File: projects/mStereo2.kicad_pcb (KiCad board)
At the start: 2 copper layers, 50.8 x 50.8 mm, 7 parts, among them J1 CONN_AMANERO, U1 ISO7240

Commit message: imported netlist to PcbNew, drew board outline and set origin
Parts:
- removed C1: 0.1, smd_transcriptic:SM0805_topbotrefs
- removed J1: CONN_AMANERO, sullins_gosselin:2x10_female
- removed MOUNT_M3.5 (x4): VAL**, mounting_transcriptic:MOUNT_M3.5
- removed U1: ISO7240, ti_gosselin:ISO7240
- added C101: 0.1, smd_gosselin:0805, F.Cu at (277.9, 56.5)
- added C102: 0.1, smd_gosselin:0805, F.Cu at (290.6, 36.2)
- added C103: 0.1, smd_gosselin:0805, F.Cu at (270.3, 61.7)
- added C104: 0.1, smd_gosselin:0805, F.Cu at (290.6, 38.8)
- added C105: 0.1, smd_gosselin:0805, F.Cu at (402.2, 45.8)
- added C106: 0.1, smd_gosselin:0805, F.Cu at (284.1, 108.4)
- added C107: 0.1, smd_gosselin:0805, F.Cu at (284.1, 105.8)
- added C201: 1, smd_gosselin:0805, F.Cu at (328.3, 105.7)
- added C202: 0.01, smd_gosselin:0805, F.Cu at (331.6, 103.1)
- added C203: 22, th_gosselin:CAP-POL-2.54-mm, F.Cu at (317.7, 105.5)
- added C301: 0.1, smd_gosselin:0805, F.Cu at (347.4, 38.8)
- added C302: 22, th_gosselin:CAP-POL-2.54-mm, F.Cu at (334.0, 53.6)
- added C303: 0.1, smd_gosselin:0805, F.Cu at (352.8, 41.4)
- added C304: 22, th_gosselin:CAP-POL-2.54-mm, F.Cu at (327.0, 53.6)
- added C305: 0.1, smd_gosselin:0805, F.Cu at (347.4, 43.9)
- added C306: 22, th_gosselin:CAP-POL-2.54-mm, F.Cu at (341.1, 41.2)
- added C307: 0.1, smd_gosselin:0805, F.Cu at (347.4, 41.4)
- added C308: 22, th_gosselin:CAP-POL-2.54-mm, F.Cu at (334.0, 41.2)
- added C309: 0.1, smd_gosselin:0805, F.Cu at (352.8, 38.8)
- added C310: 22, th_gosselin:CAP-POL-2.54-mm, F.Cu at (327.0, 41.2)
- added C311: 0.1, smd_gosselin:0805, F.Cu at (352.8, 36.2)
- added C312: 22, th_gosselin:CAP-POL-2.54-mm, F.Cu at (318.4, 54.7)
- added C401: 0.1, smd_gosselin:0805, F.Cu at (352.2, 71.2)
- added C402: 22, th_gosselin:CAP-POL-2.54-mm, F.Cu at (333.3, 88.5)
- added C403: 0.1, smd_gosselin:0805, F.Cu at (346.7, 78.9)
- added C404: 22, th_gosselin:CAP-POL-2.54-mm, F.Cu at (326.3, 88.5)
- added C405: 0.1, smd_gosselin:0805, F.Cu at (346.7, 73.8)
- added C406: 22, th_gosselin:CAP-POL-2.54-mm, F.Cu at (340.4, 76.2)
- added C407: 0.1, smd_gosselin:0805, F.Cu at (352.2, 76.3)
- added C408: 22, th_gosselin:CAP-POL-2.54-mm, F.Cu at (333.3, 76.2)
- added C409: 0.1, smd_gosselin:0805, F.Cu at (346.7, 76.3)
- added C410: 22, th_gosselin:CAP-POL-2.54-mm, F.Cu at (326.3, 76.2)
- added C411: 0.1, smd_gosselin:0805, F.Cu at (352.2, 73.8)
- added C412: 22, th_gosselin:CAP-POL-2.54-mm, F.Cu at (317.7, 89.7)
- added C501: 22, th_gosselin:CAP-POL-2.54-mm, F.Cu at (258.6, 110.8)
- added C502: 0.01, smd_gosselin:0805, F.Cu at (264.9, 114.9)
- added C503: 1, smd_gosselin:0805, F.Cu at (272.3, 110.6)
- added C601: 100, th_gosselin:CAP-POL-2.54-mm, F.Cu at (381.6, 96.5)
- added C602: 100, th_gosselin:CAP-POL-2.54-mm, F.Cu at (374.6, 96.5)
- added C603: 100, th_gosselin:CAP-POL-2.54-mm, F.Cu at (367.5, 96.5)
- added C604: 100, th_gosselin:CAP-POL-2.54-mm, F.Cu at (388.7, 96.5)
- added C605: 0.1, smd_gosselin:0805, F.Cu at (398.9, 109.3)
- added C606: 0.1, smd_gosselin:0805, F.Cu at (401.3, 91.5)
- added C607: 470p, th_gosselin:CAP-BOX-5.00-mm, F.Cu at (367.9, 107.6)
- added C608: 470p, th_gosselin:CAP-BOX-5.00-mm, F.Cu at (375.8, 107.6)
- added C701: 100, th_gosselin:CAP-POL-2.54-mm, F.Cu at (381.6, 70.5)
- added C702: 100, th_gosselin:CAP-POL-2.54-mm, F.Cu at (374.6, 70.5)
- added C703: 100, th_gosselin:CAP-POL-2.54-mm, F.Cu at (367.5, 70.5)
- added C704: 100, th_gosselin:CAP-POL-2.54-mm, F.Cu at (388.7, 70.5)
- added C705: 0.1, smd_gosselin:0805, F.Cu at (398.9, 83.3)
- added C706: 0.1, smd_gosselin:0805, F.Cu at (401.3, 65.6)
- added C707: 470p, th_gosselin:CAP-BOX-5.00-mm, F.Cu at (367.9, 81.6)
- added C708: 470p, th_gosselin:CAP-BOX-5.00-mm, F.Cu at (375.8, 81.6)
- added D101: AMBER_LED, smd_gosselin:1206_LED, F.Cu at (395.7, 41.2)
- added D102: GREEN_LED, smd_gosselin:1206_LED, F.Cu at (403.3, 37.3)
- added D103: RED_LED, smd_gosselin:1206_LED, F.Cu at (395.7, 36.9)
- added D104: GREEN_LED, smd_gosselin:1206_LED, F.Cu at (403.3, 42.1)
- added D105: GREEN_LED, smd_gosselin:1206_LED, F.Cu at (395.7, 46.0)
- added D201: GREEN_LED, smd_gosselin:1206_LED, F.Cu at (325.1, 101.7)
- added D301: RED_LED, smd_gosselin:1206_LED, F.Cu at (341.4, 49.2)
- added D401: RED_LED, smd_gosselin:1206_LED, F.Cu at (340.7, 84.2)
- added D501: GREEN_LED, smd_gosselin:1206_LED, F.Cu at (273.4, 106.9)
- added P101: CONN_AMANERO, sullins_gosselin:2x10_female, F.Cu at (261.3, 50.1)
- added P102: Screw-term 1x2, phoenix_gosselin:1x2, F.Cu at (288.8, 91.8)
- added P103: Screw-term 1X3, phoenix_gosselin:1x3, F.Cu at (290.3, 77.1)
- added P104: XLR-MALE, neutrik_gosselin:NC3MAAH-1, F.Cu at (269.2, 79.3)
- added P105: XLR-MALE, neutrik_gosselin:NC3MAAH-1, F.Cu at (378.9, 44.3)
- added R101: 121, smd_gosselin:0805, F.Cu at (372.9, 57.6)
- added R102: 121, smd_gosselin:0805, F.Cu at (389.3, 57.6)
- added R103: 121, smd_gosselin:0805, F.Cu at (367.5, 57.6)
- added R104: 825, smd_gosselin:0805, F.Cu at (383.8, 57.6)
- added R105: 825, smd_gosselin:0805, F.Cu at (378.4, 57.6)
- added R201: 121, smd_gosselin:0805, F.Cu at (331.6, 100.6)
- added R301: 121, smd_gosselin:0805, F.Cu at (347.4, 36.2)
- added R401: 121, smd_gosselin:0805, F.Cu at (346.7, 71.2)
- added R501: 121, smd_gosselin:0805, F.Cu at (272.3, 113.1)
- added R601: 1.21k, smd_gosselin:0805, F.Cu at (388.8, 103.9)
- added R602: 1.21k, smd_gosselin:0805, F.Cu at (394.3, 103.9)
- added R603: 1.21k, smd_gosselin:0805, F.Cu at (401.3, 94.1)
- added R604: 1.21k, smd_gosselin:0805, F.Cu at (394.3, 106.6)
- added R605: 2.49k, smd_gosselin:0805, F.Cu at (395.0, 98.4)
- added R606: 2.49k, smd_gosselin:0805, F.Cu at (400.5, 99.4)
- added R607: 1.21k, smd_gosselin:0805, F.Cu at (388.0, 110.8)
- added R608: 1.21k, smd_gosselin:0805, F.Cu at (393.4, 109.3)
- added R609: 1.21k, smd_gosselin:0805, F.Cu at (382.5, 110.8)
- added R610: 1.21k, smd_gosselin:0805, F.Cu at (400.5, 102.1)
- added R611: 2.49k, smd_gosselin:0805, F.Cu at (395.0, 101.1)
- added R612: 2.49k, smd_gosselin:0805, F.Cu at (399.7, 104.8)
- added R613: 10, smd_gosselin:0805, F.Cu at (388.8, 106.6)
- added R614: 10, smd_gosselin:0805, F.Cu at (401.3, 96.8)
- added R701: 1.21k, smd_gosselin:0805, F.Cu at (388.8, 78.0)
- added R702: 1.21k, smd_gosselin:0805, F.Cu at (394.3, 78.0)
- added R703: 1.21k, smd_gosselin:0805, F.Cu at (401.3, 68.2)
- added R704: 1.21k, smd_gosselin:0805, F.Cu at (394.3, 80.7)
- added R705: 2.49k, smd_gosselin:0805, F.Cu at (395.0, 72.5)
- added R706: 2.49k, smd_gosselin:0805, F.Cu at (400.5, 73.5)
- added R707: 1.21k, smd_gosselin:0805, F.Cu at (388.0, 84.9)
- added R708: 1.21k, smd_gosselin:0805, F.Cu at (393.4, 83.4)
- added R709: 1.21k, smd_gosselin:0805, F.Cu at (382.5, 84.9)
- added R710: 1.21k, smd_gosselin:0805, F.Cu at (400.5, 76.2)
- added R711: 2.49k, smd_gosselin:0805, F.Cu at (395.0, 75.2)
- added R712: 2.49k, smd_gosselin:0805, F.Cu at (399.7, 78.9)
- added R713: 10, smd_gosselin:0805, F.Cu at (388.8, 80.6)
- added R714: 10, smd_gosselin:0805, F.Cu at (401.3, 70.8)
- added U101: ISO7640, ti_gosselin:SOIC-16-W, F.Cu at (273.4, 43.1)
- added U102: CDCLVC1104, ti_gosselin:TSSOP-8, F.Cu at (283.2, 51.9)
- added U103: MCP100-315DI, microchip_gosselin:SOT-23-3, F.Cu at (395.1, 52.1)
- added U104: SRC4192, ti_gosselin:TSSOP-28, F.Cu at (283.5, 41.6)
- added U201: LT1761, linear_gosselin:SOT-23-5, F.Cu at (323.4, 107.5)
- added U301: WM8741, ti_gosselin:TSSOP-28, F.Cu at (319.1, 41.6)
- added U401: WM8741, ti_gosselin:TSSOP-28, F.Cu at (318.5, 76.6)
- added U501: LT1763, linear_gosselin:SOIC-8, F.Cu at (265.8, 109.1)
- added U601: OPA1632, ti_gosselin:MSOP-8-PWP, F.Cu at (382.9, 106.1)
- added U602: OPA1632, ti_gosselin:MSOP-8-PWP, F.Cu at (395.4, 93.7)
- added U701: OPA1632, ti_gosselin:MSOP-8-PWP, F.Cu at (382.9, 80.1)
- added U702: OPA1632, ti_gosselin:MSOP-8-PWP, F.Cu at (395.4, 67.8)
- added X101: XTAL, crystek_gosselin:XTAL-5x7mm, F.Cu at (271.3, 55.4)
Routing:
- net /VCC1: track 20.4 -> 0.00 mm
- net /GND1: track 19.6 -> 0.00 mm
- net Net-(J1-Pad2): track 15.9 -> 0.00 mm
- net Net-(J1-Pad3): track 15.3 -> 0.00 mm
- net Net-(J1-Pad4): track 14.7 -> 0.00 mm
- removed copper zone on B.Cu, net (none)
- removed copper zone on F.Cu, net (none)
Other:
- board size 50.8 x 50.8 mm -> 220 x 160 mm
- net class Default: clearance 0.127 -> 0.254; trace_width 0.1524 -> 0.254; via_dia 0.635 -> 0.889; via_drill 0.381 -> 0.635
- net class Power removed
- rule trace_clearance: 0.127 -> 0.254
- rule trace_min: 0.127 -> 0.254
- rule via_min_drill: 0.254 -> 0.508
- rule via_min_size: 0.254 -> 0.889
- board text removed: "board origin"

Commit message: prelimiary component positioning, board resizing, added mounting holes footprint
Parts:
- added mounting_m3: VAL**, mounting_gosselin:mounting_m3, F.Cu at (38.8, 38.8)
- added mounting_m3: VAL**, mounting_gosselin:mounting_m3, F.Cu at (190.7, 38.8)
- added mounting_m3: VAL**, mounting_gosselin:mounting_m3, F.Cu at (38.8, 151.2)
- added mounting_m3: VAL**, mounting_gosselin:mounting_m3, F.Cu at (190.7, 151.2)
- added mounting_m3: VAL**, mounting_gosselin:mounting_m3, F.Cu at (100.0, 116.8)
- added mounting_m3: VAL**, mounting_gosselin:mounting_m3, F.Cu at (100.0, 141.8)
- added mounting_m3: VAL**, mounting_gosselin:mounting_m3, F.Cu at (40.0, 141.8)
- added mounting_m3: VAL**, mounting_gosselin:mounting_m3, F.Cu at (40.0, 116.8)
- P101: moved to B.Cu
- moved D104 363.2 mm to (41.4, 72.8), turned to 180 degrees
- moved D102 363.1 mm to (41.4, 66.8)
- moved D103 355.1 mm to (41.4, 60.9)
- moved D105 354.8 mm to (41.4, 63.9)
- moved D101 354.5 mm to (41.4, 51.9)
- moved C105 341.7 mm to (65.5, 103.6)
- moved R102 341.5 mm to (47.9, 66.8)
- moved U103 338.8 mm to (60.4, 104.8)
- moved R104 336.3 mm to (47.9, 72.8), turned to 180 degrees
- moved R105 330.5 mm to (47.9, 63.9)
- moved R101 325.1 mm to (47.9, 51.9)
- moved R103 319.6 mm to (47.9, 60.9)
- moved D401 300.7 mm to (41.4, 54.9)
- moved R301 300.2 mm to (47.9, 57.9)
- moved D301 300.1 mm to (41.4, 57.9)
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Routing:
- added copper zone on InnerB.Cu, net +12V
- added copper zone on B.Cu, net +5V
- added copper zone on B.Cu, net -12V
- added copper zone on InnerF.Cu, net DGND
- added copper zone on InnerF.Cu, net GNDA
- added copper zone on InnerB.Cu, net VAA
- added copper zone on InnerB.Cu, net VDD
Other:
- board size 220 x 160 mm -> 159.5 x 120 mm
- copper layers 2 -> 4

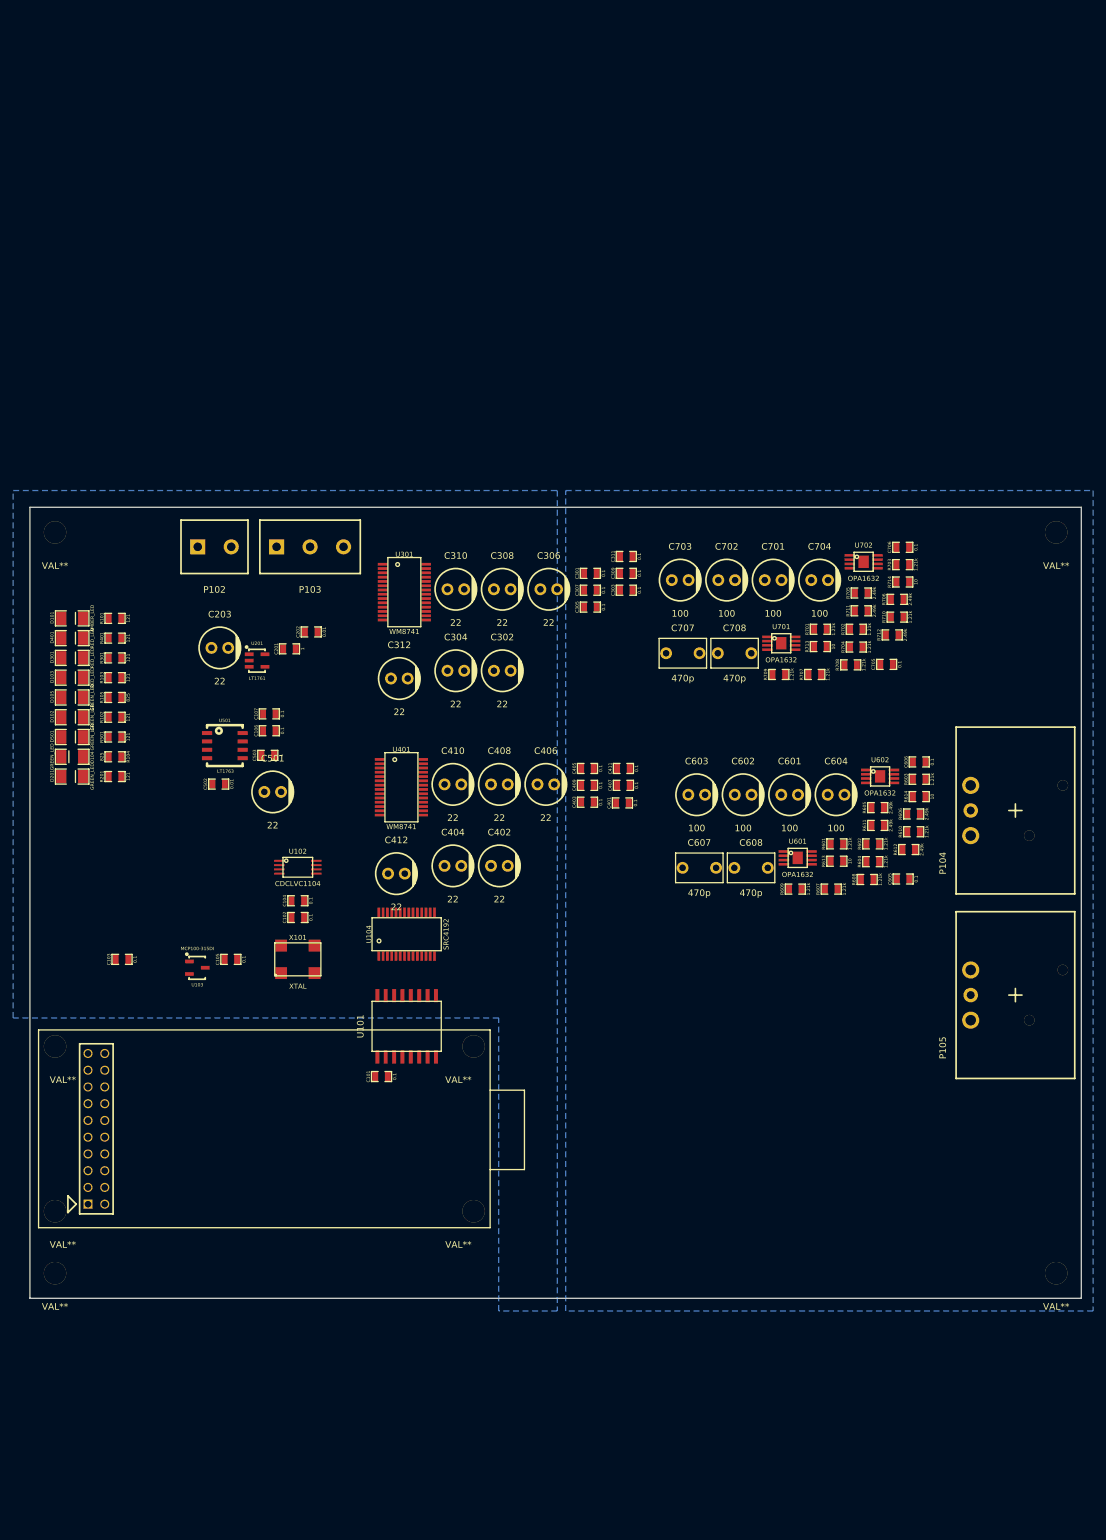
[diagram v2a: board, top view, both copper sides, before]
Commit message: secondary part positioning (DAC, filters)
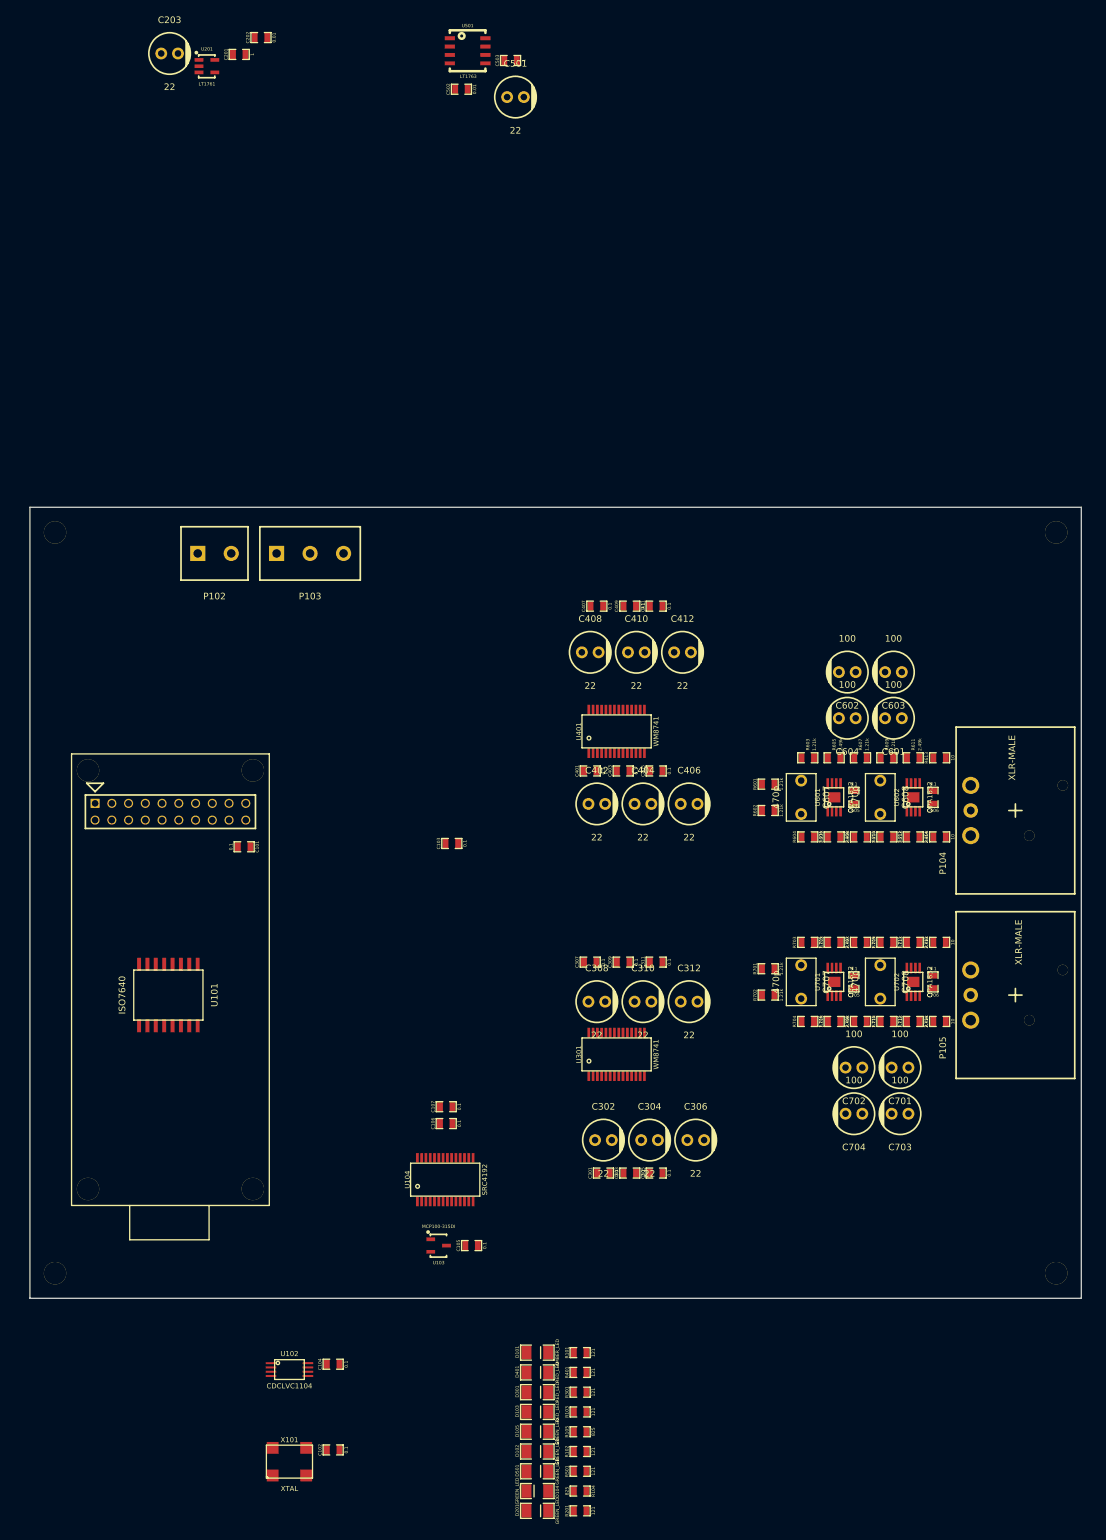
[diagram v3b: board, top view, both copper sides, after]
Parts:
- moved D101 131.9 mm to (112.0, 163.2)
- moved D102 131.9 mm to (112.0, 178.2)
- moved D103 131.9 mm to (112.0, 172.2)
- moved D104 131.9 mm to (112.0, 184.2)
- moved D105 131.9 mm to (112.0, 175.2)
- moved D201 131.9 mm to (112.0, 187.2)
- moved D301 131.9 mm to (112.0, 169.2)
- moved D401 131.9 mm to (112.0, 166.2)
- moved D501 131.9 mm to (112.0, 181.2)
- moved R101 131.9 mm to (118.5, 163.2)
- moved R102 131.9 mm to (118.5, 178.2)
- moved R103 131.9 mm to (118.5, 172.2)
- moved R104 131.9 mm to (118.5, 184.2)
- moved R105 131.9 mm to (118.5, 175.2)
- moved R201 131.9 mm to (118.5, 187.2)
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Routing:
- removed copper zone on InnerB.Cu, net +12V
- removed copper zone on B.Cu, net +5V
- removed copper zone on B.Cu, net -12V
- removed copper zone on InnerF.Cu, net DGND
- removed copper zone on InnerF.Cu, net GNDA
- removed copper zone on InnerB.Cu, net VAA
- removed copper zone on InnerB.Cu, net VDD
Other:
- board text added: "Add board notes (i.e. voltage labels, date, rev, name, etc.)"
- board text added: "Annotations: dimensions, origin, coord +ve directions"
- board text added: "Change paper size to letter"
- board text added: "Key part info (ie xtal feq., connector part no's and channel L/R)"
- board text added: "Key part info (ie xtal freq. connect channels L/R etc.)"
- board text added: "Set design rules"
- board text added: "TODO's:"

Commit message: add mfg. spec. info; add dwg. info to sheet text feilds
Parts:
- moved C102 91.9 mm to (94.0, 87.0)
- moved C104 91.9 mm to (94.0, 74.0)
- moved X101 89.5 mm to (93.7, 92.4), turned to 180 degrees
- moved P103 76.4 mm to (153.9, 40.3)
- moved P102 73.9 mm to (136.9, 40.3)
- moved U102 70.3 mm to (93.7, 98.2)
- moved C103 54.2 mm to (66.0, 129.0)
- moved U104 31.1 mm to (93.7, 106.2), turned to 270 degrees
- moved U401 23.6 mm to (109.3, 87.5)
- moved U101 21.1 mm to (77.0, 107.3), turned to 0 degrees
- moved U301 15.1 mm to (109.3, 114.4)
- moved C106 3.19 mm to (101.3, 128.0)
- moved C107 3.14 mm to (101.3, 125.9)
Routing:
- net /DATA_2: track 0.00 -> 11.8 mm
- net /BCLK_2: track 0.00 -> 10.8 mm
- net /LRCLK_2: track 0.00 -> 9.61 mm
- net /DAC_L/DATA: track 0.00 -> 8.75 mm
- net /DAC_L/LRCLK: track 0.00 -> 7.18 mm
- net /DAC_R/MCLK: track 0.00 -> 6.65 mm
- net /DAC_L/MCLK: track 0.00 -> 6.45 mm
- net /DAC_L/BCLK: track 0.00 -> 5.64 mm
- net /SRC_MCLK: track 0.00 -> 4.62 mm
- net Net-(U102-Pad1): track 0.00 -> 2.87 mm
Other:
- net class Default: clearance 0.254 -> 0.2032; trace_width 0.254 -> 0.3048
- rule trace_clearance: 0.254 -> 0.2032
- rule trace_min: 0.254 -> 0.1524
- rule via_min_drill: 0.508 -> 0.2032
- rule via_min_size: 0.889 -> 0.2032
- board text added: "1) min trace/space 0.006 in. 2) Min. hole (finished) 0.008 in. 3) Max. hole (non-plated) 199 mils 4) Min. SMT pad spacing 0.005 in. 5) Min. annular ring 0.005 in. 6) Min. drill-to-copper space 0.008 in. 7) Min. edge-to-copper space 0.008 in."
- board text added: "Make keepout for a USB jack near XLR connectors"
- board text added: "PCB Fab Express Process Specs:"
- board text added: "Place test points"
- board text added: "Try building with a trace-length measurement tool"
- board text removed: "Change paper size to letter"
- board text removed: "Set design rules"

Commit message: reposition parts, start routing, add notes for next rev. changes to /doc folder
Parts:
- moved D201 152.8 mm to (76.0, 38.7), turned to 270 degrees
- moved D104 149.2 mm to (79.0, 38.7), turned to 90 degrees
- moved R201 148.3 mm to (76.0, 45.2), turned to 270 degrees
- moved D501 145.7 mm to (82.0, 38.7), turned to 270 degrees
- moved R104 144.5 mm to (79.0, 45.2), turned to 90 degrees
- moved R501 140.8 mm to (82.0, 45.2), turned to 270 degrees
- moved D102 140.0 mm to (99.9, 38.7), turned to 270 degrees
- moved D105 139.2 mm to (85.0, 38.7), turned to 270 degrees
- moved D103 135.7 mm to (88.0, 38.7), turned to 270 degrees
- moved R102 134.3 mm to (99.9, 45.2), turned to 270 degrees
- moved R105 134.3 mm to (85.0, 45.2), turned to 270 degrees
- moved D301 132.2 mm to (91.0, 38.7), turned to 270 degrees
- moved R103 130.7 mm to (88.0, 45.2), turned to 270 degrees
- moved D401 128.8 mm to (94.0, 38.7), turned to 270 degrees
- moved R301 127.1 mm to (91.0, 45.2), turned to 270 degrees
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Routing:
- net /DATA_1: track 0.00 -> 62.3 mm
- net DGND: track 0.00 -> 60.5 mm, vias 0 -> 21
- net /BCLK_1: track 0.00 -> 60.4 mm
- net /LRCLK_1: track 0.00 -> 58.6 mm
- net VDD: track 0.00 -> 42.9 mm, vias 0 -> 9
- net /FILTER_R/VIN-: track 0.00 -> 29.4 mm, vias 0 -> 2
- net VCC: track 0.00 -> 28.5 mm
- net /FILTER_R/VIN+: track 0.00 -> 24.5 mm
- net +5V: track 0.00 -> 18.1 mm, vias 0 -> 3
- net Net-(C405-Pad1): track 0.00 -> 14.6 mm
- net /DAC_L/BCLK: track 5.64 -> 18.9 mm, vias 0 -> 1
- net /DAC_L/DATA: track 8.75 -> 20.9 mm, vias 0 -> 1
- net /DAC_L/LRCLK: track 7.18 -> 18.7 mm, vias 0 -> 1
- net Net-(D103-Pad1): track 0.00 -> 9.85 mm, vias 0 -> 2
- net /FILTER_L/VIN-: track 0.00 -> 9.74 mm
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- added copper zone on InnerB.Cu, net +12V
- added copper zone on InnerB.Cu, net +5V
- added copper zone on B.Cu, net -12V
- added copper zone on InnerF.Cu, net DGND
- added copper zone on InnerF.Cu, net GNDA
- added copper zone on InnerB.Cu, net VAA
- added copper zone on B.Cu, net VDD
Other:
- board text added: "LEFT"
- board text added: "Labels for LED indicators"
- board text added: "RIGHT"
- board text added: "Reposition part info so its readable"
- board text added: "Text for Amanero Combo 384"
- board text removed: "Place test points"
- board text removed: "Try building with a trace-length measurement tool"
